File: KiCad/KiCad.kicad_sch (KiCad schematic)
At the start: 31 parts, among them J1 DC-IN, J2 TYPE-C, J3 Conn_01x03_Pin, SW1 TS665CJ, SW2 TS665CJ, U1 ESP32-WROOM-32E, U2 MP1584EN, U3 CH340C, U4 RT9013-33GB, U5 DM-OLED096-636

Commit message: 增加0.96'OLED(已完成原理圖及PCB)及開始測試按鈕(只添加到PCB，原理圖未連接)
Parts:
- added C11: 0.1uF, Capacitor_SMD:C_0603_1608Metric, symbol Device:C
- SW1: value TS665CJ -> reset
- SW2: value TS665CJ -> start
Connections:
- net +3V3: now also U5.2 (VCC_IN), C11.1
- net GND: now also U5.1 (GND), C11.2
- net SDA: now reaches U1.33 (IO21)
- net SDA: now also U5.3 (SCL)
- net SCL: now reaches U1.36 (IO22)
- net SCL: now also U5.4 (SDA)

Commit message: 完成start按鈕的原理圖/PCB連接
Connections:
- net GND: now also SW2.3 (C), SW2.4 (D)
- net start: now reaches SW2.1 (A)
- net start: now also U1.23 (IO15)
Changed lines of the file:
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@@
 	)
 	(junction
+		(at 170.18 33.02)
+		(diameter 0)
+		(color 0 0 0 0)
+	)
+	(junction
 		(at 95.25 167.64)
 		(diameter 0)
@@
 	(wire
 		(pts
+			(xy 170.18 33.02) (xy 185.42 33.02)
+		)
+		(stroke
+			(width 0)
+			(type default)
+		)
+	)
+	(wire
+		(pts
 			(xy 101.6 170.18) (xy 101.6 182.88)
 		)
@@
 	(wire
 		(pts
+			(xy 72.39 50.8) (xy 80.01 50.8)
+		)
+		(stroke
+			(width 0)
+			(type default)
+		)
+	)
+	(wire
+		(pts
 			(xy 201.93 72.39) (xy 201.93 74.93)
 		)
@@
 	(wire
 		(pts
+			(xy 162.56 27.94) (xy 170.18 27.94)
+		)
+		(stroke
+			(width 0)
+			(type default)
+		)
+	)
+	(wire
+		(pts
 			(xy 181.61 129.54) (xy 181.61 125.73)
 		)
@@
 		)
 	)
+	(label "start"
+		(at 162.56 27.94 0)
+		(effects
+			(font
+				(size 1.27 1.27)
+			)
+			(justify left bottom)
+		)
+	)
+	(label "start"
+		(at 74.93 50.8 0)
+		(effects
+			(font
+				(size 1.27 1.27)
+			)
+			(justify left bottom)
+		)
+	)
 	(label "D+"
 		(at 179.07 129.54 180)
@@
 					(unit 1)
 				)
+			)
+		)
+	)
+	(symbol
+		(lib_id "power:GND")
+		(at 170.18 33.02 0)
+		(unit 1)
+		(exclude_from_sim no)
+		(in_bom yes)
+		(on_board yes)
+		(dnp no)
+		(fields_autoplaced yes)
+		(property "Reference" "#PWR036"
+			(at 170.18 39.37 0)
+			(effects
+				(font
+					(size 1.27 1.27)
+				)
+				(hide yes)
+			)
+		)
+		(property "Value" "GND"
+			(at 170.18 38.1 0)
+			(effects
+				(font
+					(size 1.27 1.27)
+				)
+			)
+		)
+		(property "Footprint" ""
+			(at 170.18 33.02 0)
+			(effects
+				(font
+					(size 1.27 1.27)
+				)
+				(hide yes)
+			)
+		)
+		(property "Datasheet" ""
+			(at 170.18 33.02 0)
+			(effects
+				(font
+					(size 1.27 1.27)
+				)
+				(hide yes)
+			)
+		)
+		(property "Description" "Power symbol creates a global label with name \"GND\" , ground"
+			(at 170.18 33.02 0)
+			(effects
+				(font
+					(size 1.27 1.27)
+				)
+				(hide yes)
+			)
+		)
+		(pin "1"
+		)
+		(instances
+			(project "KiCad"
+				(path "/8145d5a2-4aff-47fb-b6a2-0059c8017b6c"
+					(reference "#PWR036")
+					(unit 1)
+				)

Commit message: 修正OLED之SDA/SCL連接錯誤
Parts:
- added U6: INA219AxDCN, Package_TO_SOT_SMD:SOT-23-8, symbol Sensor_Energy:INA219AxDCN
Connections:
- net SCL: now also U5.3 (SCL); no longer U5.4 (SDA)
- net SDA: now also U5.4 (SDA); no longer U5.3 (SCL)
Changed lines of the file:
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@@
-		)
-	)
-	(label "SCL"
-		(at 190.5 69.85 0)
-		(effects
-			(font
-				(size 1.27 1.27)
-			)
-			(justify left bottom)
 		)
 	)
@@
 	)
 	(label "SDA"
-		(at 190.5 67.31 0)
+		(at 190.5 69.85 0)
 		(effects
 			(font
@@
 		)
 	)
+	(label "SCL"
+		(at 190.5 67.31 0)
+		(effects
+			(font
+				(size 1.27 1.27)
+			)
+			(justify left bottom)
+		)
+	)
 	(label "start"
 		(at 162.56 27.94 0)
@@
 					(unit 1)
 				)
+			)
+		)
+	)
+	(symbol
+		(lib_id "Sensor_Energy:INA219AxDCN")
+		(at 120.65 59.69 0)
+		(unit 1)
+		(exclude_from_sim no)
+		(in_bom yes)
+		(on_board yes)
+		(dnp no)
+		(fields_autoplaced yes)
+		(property "Reference" "U6"
+			(at 122.7933 46.99 0)
+			(effects
+				(font
+					(size 1.27 1.27)
+				)
+				(justify left)
+			)
+		)
+		(property "Value" "INA219AxDCN"
+			(at 122.7933 49.53 0)
+			(effects
+				(font
+					(size 1.27 1.27)
+				)
+				(justify left)
+			)
+		)
+		(property "Footprint" "Package_TO_SOT_SMD:SOT-23-8"
+			(at 137.16 68.58 0)
+			(effects
+				(font
+					(size 1.27 1.27)
+				)
+				(hide yes)
+			)
+		)
+		(property "Datasheet" "http://www.ti.com/lit/ds/symlink/ina219.pdf"
+			(at 129.54 62.23 0)
+			(effects
+				(font
+					(size 1.27 1.27)
+				)
+				(hide yes)
+			)
+		)
+		(property "Description" "Zero-Drift, Bidirectional Current/Power Monitor (0-26V) With I2C Interface, SOT-23-8"
+			(at 120.65 59.69 0)
+			(effects
+				(font
+					(size 1.27 1.27)
+				)
+				(hide yes)
+			)
+		)
+		(pin "7"
+		)
+		(pin "6"
+		)
+		(pin "8"
+		)
+		(pin "5"
+		)
+		(pin "4"
+		)
+		(pin "1"
+		)
+		(pin "3"
+		)
+		(pin "2"
+		)
+		(instances
+			(project ""
+				(path "/8145d5a2-4aff-47fb-b6a2-0059c8017b6c"
+					(reference "U6")
+					(unit 1)
+				)

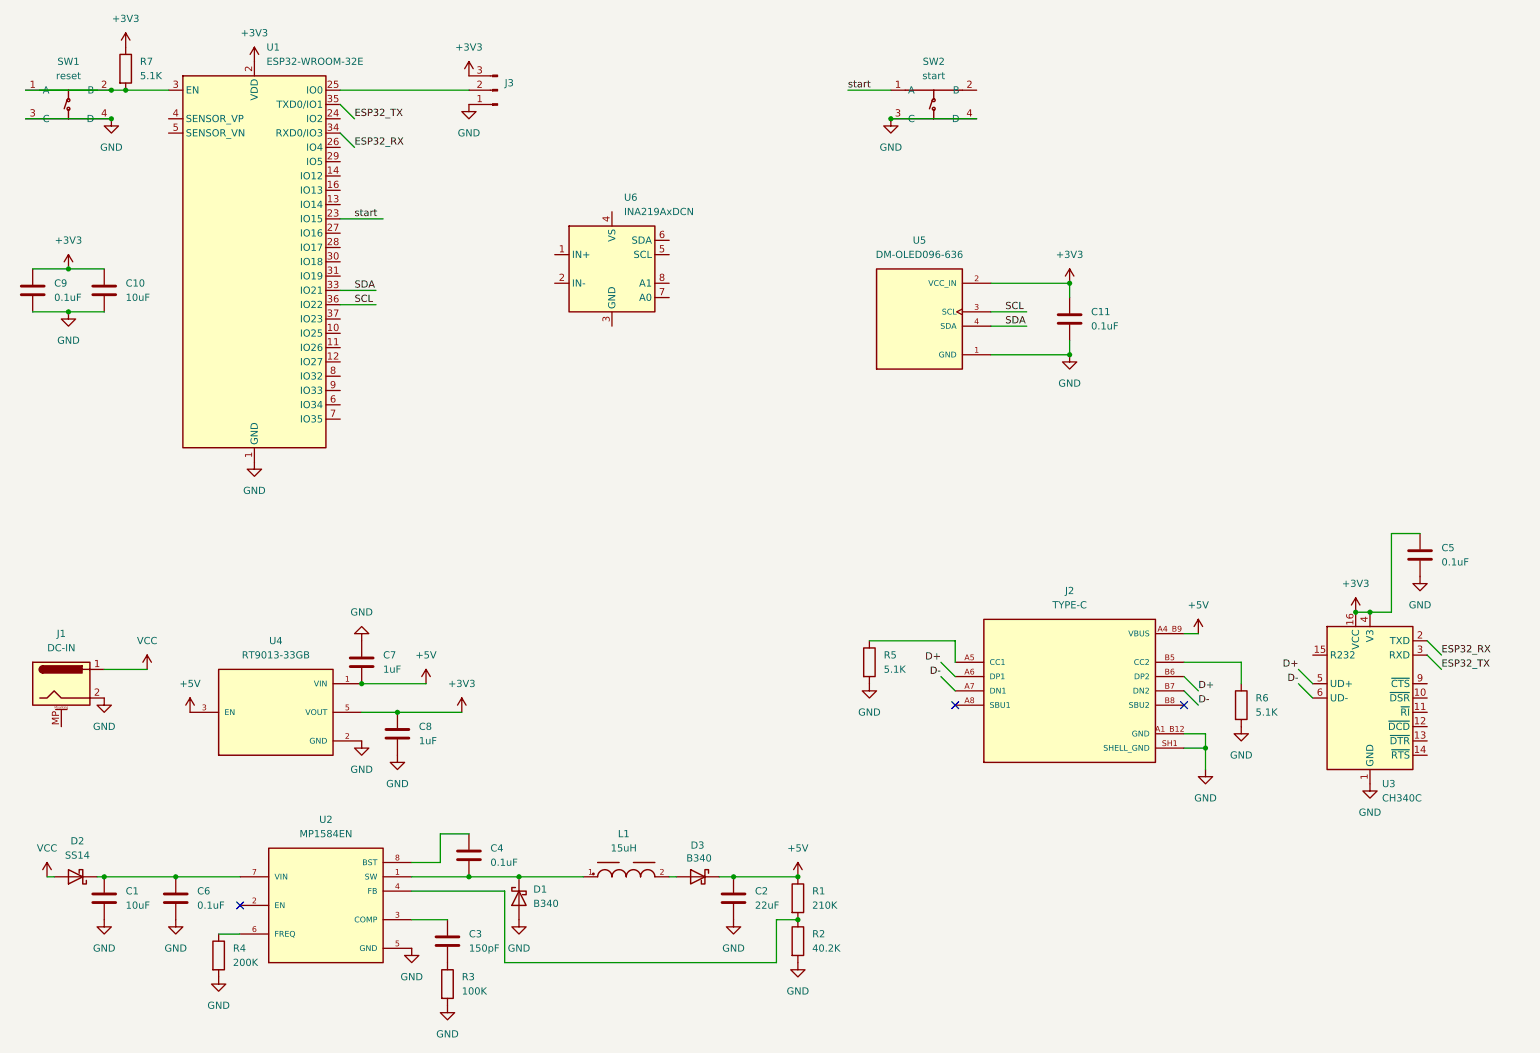
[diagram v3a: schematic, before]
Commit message: 連接功率計IC的供電，新增MOS及驅動IC(未連接)
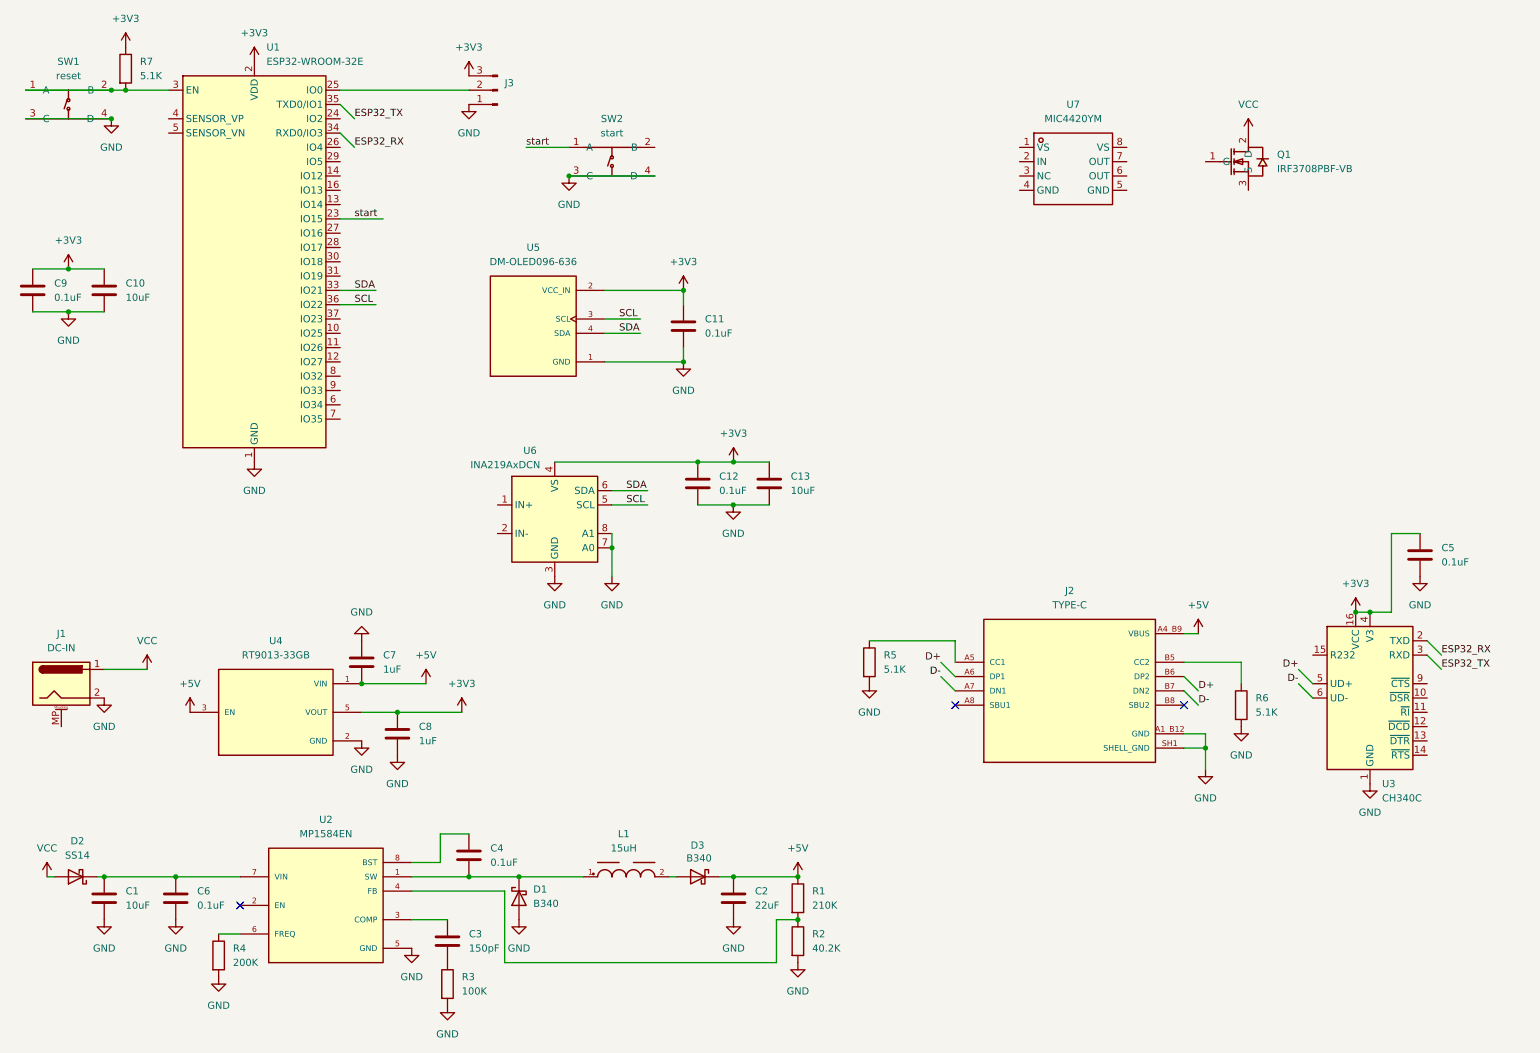
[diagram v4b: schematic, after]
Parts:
- added C12: 0.1uF, Capacitor_SMD:C_0603_1608Metric, symbol Device:C
- added C13: 10uF, Capacitor_SMD:C_0603_1608Metric, symbol Device:C
- added Q1: IRF3708PBF-VB, IRF3708:TO-220-3_L10.0-W4.6-P2.54-L, symbol IRF3708:IRF3708PBF-VB
- added U7: MIC4420YM, MIC4420YM:SOIC-8_L4.9-W3.9-P1.27-LS6.0-BL, symbol MIC4420YM:MIC4420YM
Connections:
- net +3V3: now also U6.4 (VS), C12.1, C13.1
- net GND: now also U6.3 (GND), U6.7 (A0), U6.8 (A1), C12.2, C13.2
- net SCL: now also U6.5 (SCL)
- net SDA: now also U6.6 (SDA)
- net VCC: now also Q1.2 (D)
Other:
- moved on the sheet: C11, SW2, U5, U6

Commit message: 完成pcb(除了DAC部分)
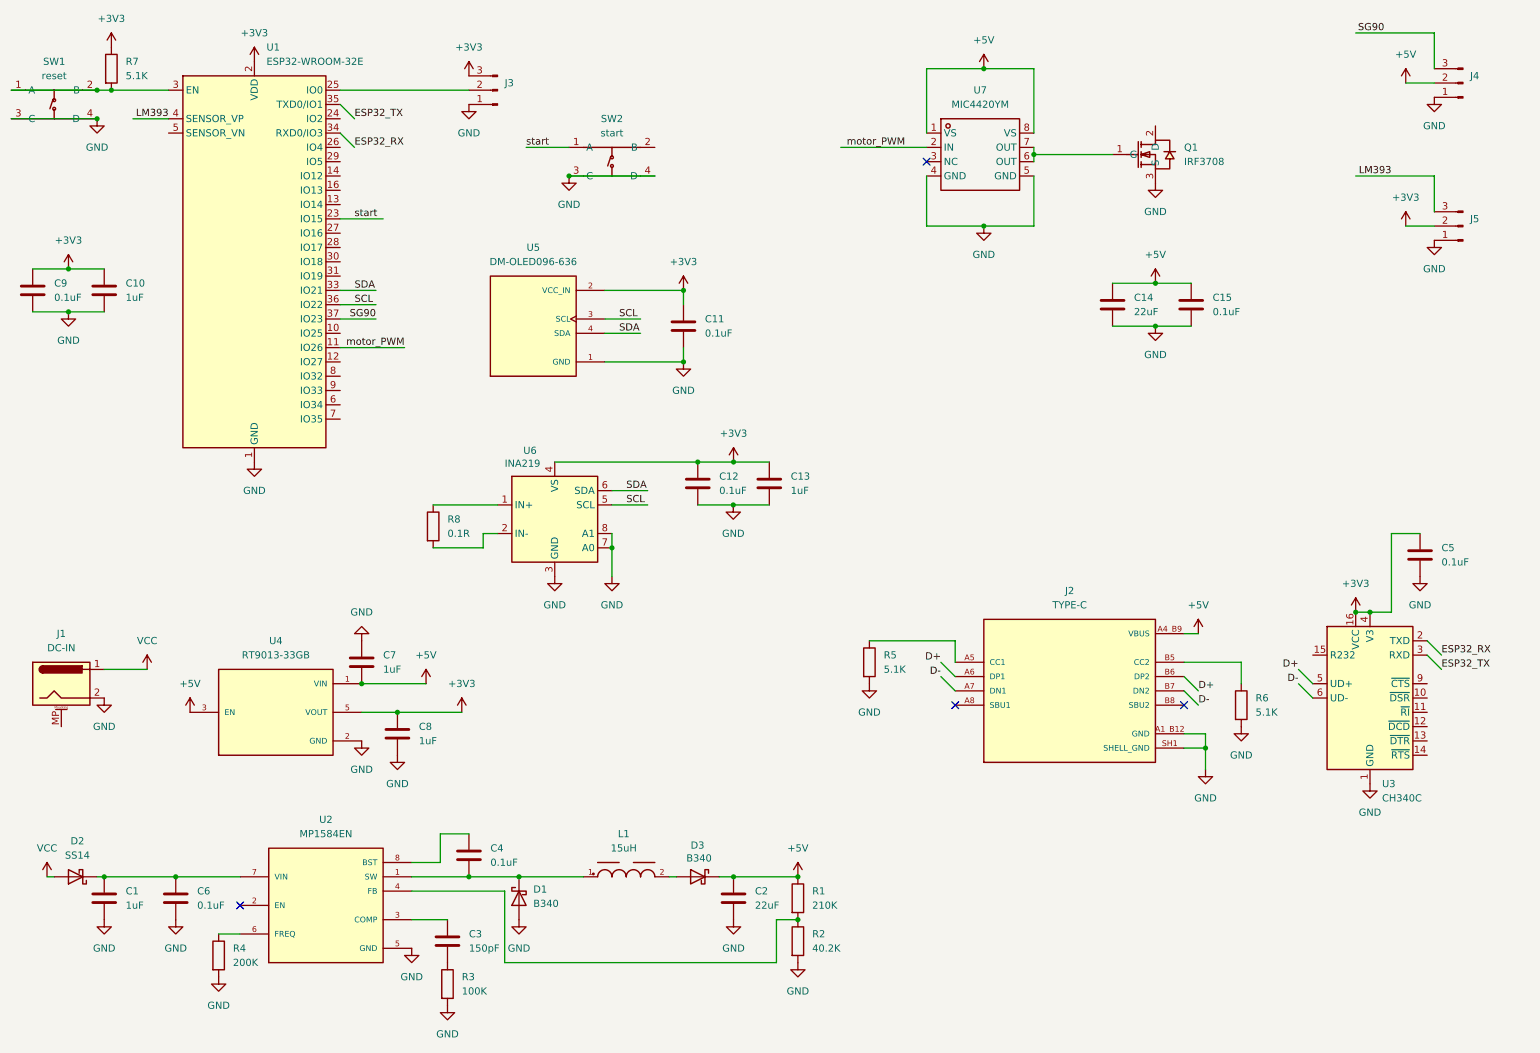
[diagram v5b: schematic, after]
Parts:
- added C14: 22uF, Capacitor_SMD:C_0805_2012Metric, symbol Device:C
- added C15: 0.1uF, Capacitor_SMD:C_0603_1608Metric, symbol Device:C
- added J4, J5: Conn_01x03_Pin, Connector_PinHeader_2.54mm:PinHeader_1x03_P2.54mm_Vertical, symbol Connector:Conn_01x03_Pin
- added R8: 0.1R, Resistor_SMD:R_2512_6332Metric, symbol Device:R
- C1, C10, C13: value 10uF -> 1uF
- Q1: value IRF3708PBF-VB -> IRF3708
- U6: value INA219AxDCN -> INA219
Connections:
- net +3V3: now also J5.2 (Pin_2)
- net +5V: now also U7.1 (VS), U7.8 (VS), C14.1, C15.1, J4.2 (Pin_2)
- net GND: now also Q1.3 (S), U7.4 (GND), U7.5 (GND), C14.2, C15.2, J4.1 (Pin_1), J5.1 (Pin_1)
- net VCC: no longer Q1.2 (D)
- net at U6.1 (IN+): now also R8.1
- net at U6.2 (IN-): now also R8.2
- net at Q1.1 (G): now also U7.6 (OUT), U7.7 (OUT)
- net motor_PWM: now reaches U7.2 (IN)
- net motor_PWM: now also U1.11 (IO26)
- net SG90: now reaches U1.37 (IO23)
- net SG90: now also J4.3 (Pin_3)
- net LM393: now reaches U1.4 (SENSOR_VP)
- net LM393: now also J5.3 (Pin_3)
- no-connect marks 3 -> 4
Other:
- moved on the sheet: Q1, R7, SW1, U7

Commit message: 補全功率測量迴路之電路
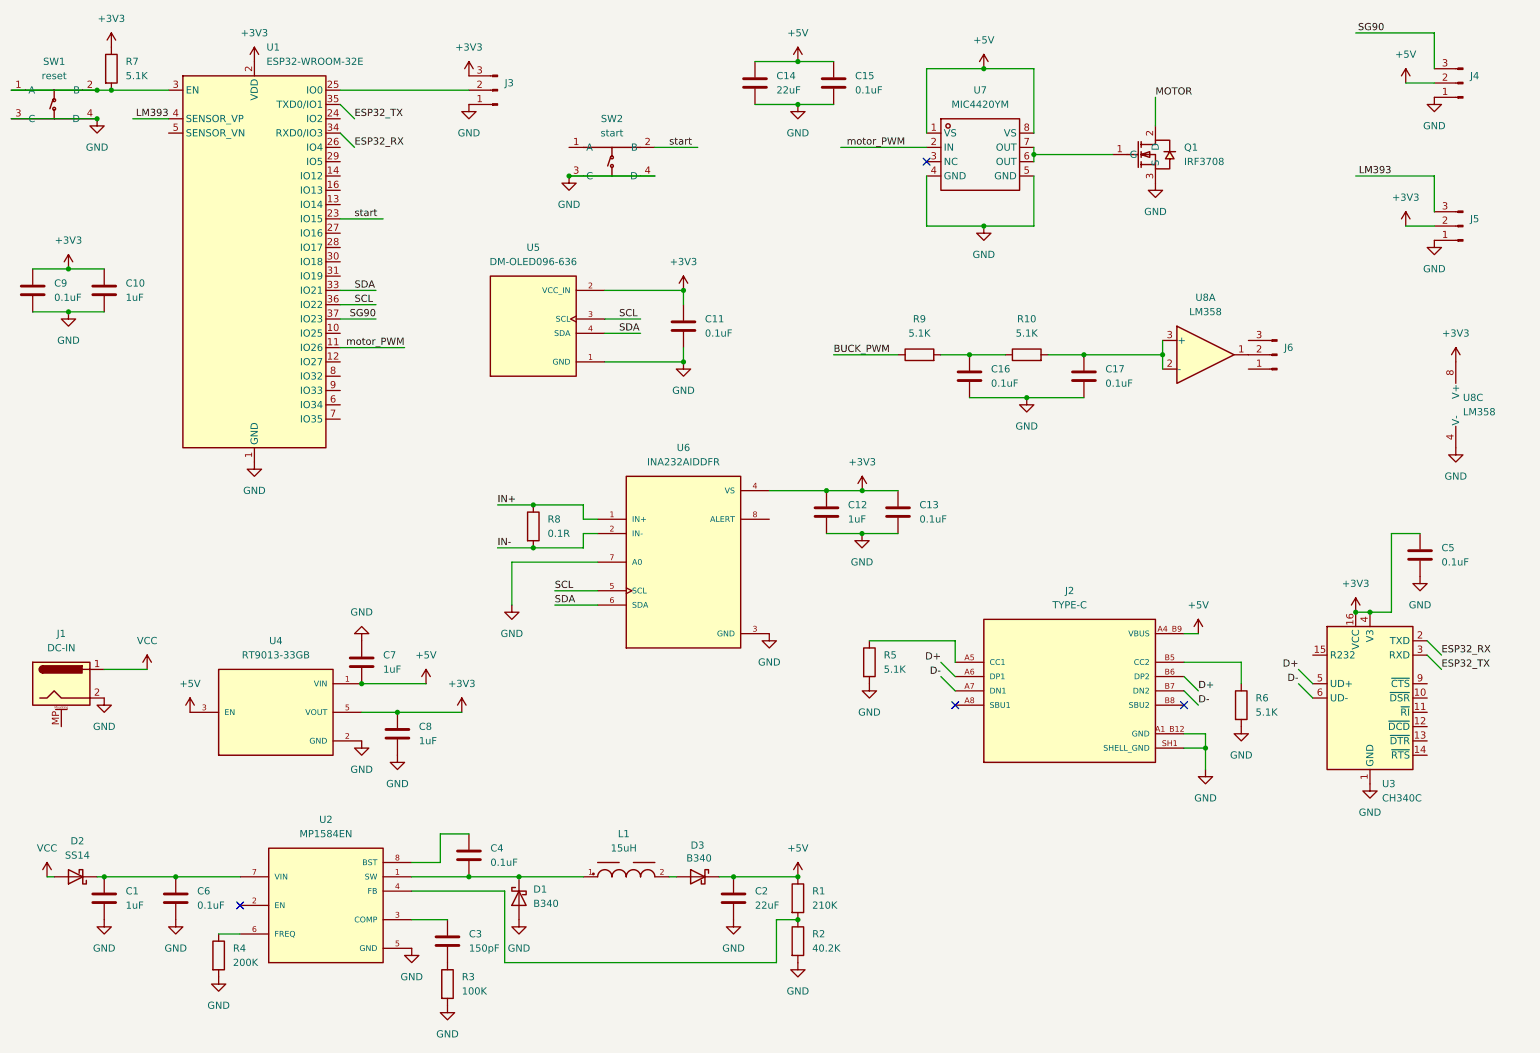
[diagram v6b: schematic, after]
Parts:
- removed U6: INA219, Package_TO_SOT_SMD:SOT-23-8, symbol Sensor_Energy:INA219AxDCN
- added C16, C17: 0.1uF, Capacitor_SMD:C_0603_1608Metric, symbol Device:C
- added J6: Conn_01x03_Pin, Connector_PinHeader_2.54mm:PinHeader_1x03_P2.54mm_Vertical, symbol Connector:Conn_01x03_Pin
- added R10, R9: 5.1K, Resistor_SMD:R_0603_1608Metric, symbol Device:R
- added U6: INA232AIDDFR, INA232AIDDFR:SOT65P280X110-8N, symbol INA232AIDDFR:INA232AIDDFR
- added U8: LM358, Package_SO:SOIC-8_5.3x6.2mm_P1.27mm, symbol Amplifier_Operational:LM358
- C12: value 0.1uF -> 1uF
- C13: value 1uF -> 0.1uF
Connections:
- net +3V3: now also U6.4 (VS), U8.8 (V+)
- net GND: now also C16.2, C17.2, U6.3 (GND), U6.7 (A0), U8.4 (V-)
- net SCL: now also U6.5 (SCL)
- net SDA: now also U6.6 (SDA)
- net start: now also SW2.2 (B); no longer SW2.1 (A)
- net IN+: now reaches R8.1
- net IN+: now also U6.1 (IN+)
- net IN-: now reaches R8.2
- net IN-: now also U6.2 (IN-)
- net MOTOR: now reaches Q1.2 (D)
- new net: C16.1, R10.1, R9.2
- new net: J6.2 (Pin_2), U8.1
- new net: C17.1, R10.2, U8.2 (-), U8.3 (+)
- new net BUCK_PWM: R9.1
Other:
- moved on the sheet: C12, C13, C14, C15, R8
